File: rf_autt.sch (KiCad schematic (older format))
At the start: 10 parts

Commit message: Fix grounding in rf autt
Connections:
- net labels removed: GNDD
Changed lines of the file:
@@
 $Descr A4 11693 8268
 encoding utf-8
-Sheet 8 9
+Sheet 7 7
 Title "HF-SDR RF-Attenuator"
 Date "2020 december"
@@
 F 3 "" H 5600 4400 50  0001 C CNN
 	1    5600 4400
-	1    0    0    -1
-$EndComp
-$Comp
-L power:GNDD #PWR?
-U 1 1 5FE533AF
-P 5600 2700
-F 0 "#PWR?" H 5600 2450 50  0001 C CNN
-F 1 "GNDD" H 5604 2545 50  0000 C CNN
-F 2 "" H 5600 2700 50  0001 C CNN
-F 3 "" H 5600 2700 50  0001 C CNN
-	1    5600 2700
 	1    0    0    -1
 $EndComp
@@
 Wire Wire Line
 	5150 1400 4400 1400
-$Comp
-L power:GNDD #PWR?
-U 1 1 5FECD05D
-P 6300 1550
-F 0 "#PWR?" H 6300 1300 50  0001 C CNN
-F 1 "GNDD" H 6304 1395 50  0000 C CNN
-F 2 "" H 6300 1550 50  0001 C CNN
-F 3 "" H 6300 1550 50  0001 C CNN
-	1    6300 1550
-	1    0    0    -1
-$EndComp
 Wire Wire Line
 	6300 1550 6300 1400
@@
 Wire Wire Line
 	6050 1550 6300 1550
-Connection ~ 6300 1550
 Text Notes 4350 1150 0    50   ~ 0
 S0    S1    Att\n\n 0     0     0dB\n 0     1    10dB\n 1     0    20dB\n 1     1    30dB
@@
 Wire Bus Line
 	4400 2150 4400 6050
+$Comp
+L power:GNDA #PWR?
+U 1 1 5FF9D7B5
+P 5600 2700
+F 0 "#PWR?" H 5600 2450 50  0001 C CNN
+F 1 "GNDA" H 5605 2527 50  0000 C CNN
+F 2 "" H 5600 2700 50  0001 C CNN
+F 3 "" H 5600 2700 50  0001 C CNN
+	1    5600 2700
+	1    0    0    -1
+$EndComp
+$Comp
+L power:GNDA #PWR?
+U 1 1 5FF9DC72
+P 6300 1550
+F 0 "#PWR?" H 6300 1300 50  0001 C CNN
+F 1 "GNDA" H 6305 1377 50  0000 C CNN
+F 2 "" H 6300 1550 50  0001 C CNN
+F 3 "" H 6300 1550 50  0001 C CNN
+	1    6300 1550
+	1    0    0    -1
+$EndComp
+Connection ~ 6300 1550
 $EndSCHEMATC

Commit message: Initalize receiver test circuit
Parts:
- gave numbers to parts that had none: 10
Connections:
- net labels added: +5VA
- net labels removed: VCC
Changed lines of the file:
@@
 OUT
 $Comp
-L sdr:FST3253 U?
+L sdr:FST3253 U4
 U 1 1 5FE50A6B
 P 5600 1900
-F 0 "U?" H 5350 2550 50  0000 C CNN
+F 0 "U4" H 5350 2550 50  0000 C CNN
 F 1 "FST3253" H 5800 2550 50  0000 C CNN
 F 2 "" H 5600 1900 50  0001 C CNN
@@
 ATT_SEL1
 $Comp
-L power:GNDA #PWR?
+L power:GNDA #PWR0136
 U 1 1 5FE53082
 P 5600 4400
-F 0 "#PWR?" H 5600 4150 50  0001 C CNN
+F 0 "#PWR0136" H 5600 4150 50  0001 C CNN
 F 1 "GNDA" H 5605 4227 50  0000 C CNN
 F 2 "" H 5600 4400 50  0001 C CNN
@@
 $EndComp
 $Comp
-L power:VCC #PWR?
-U 1 1 5FE54C36
-P 5600 1200
-F 0 "#PWR?" H 5600 1050 50  0001 C CNN
-F 1 "VCC" H 5615 1373 50  0000 C CNN
-F 2 "" H 5600 1200 50  0001 C CNN
-F 3 "" H 5600 1200 50  0001 C CNN
-	1    5600 1200
-	1    0    0    -1
-$EndComp
-$Comp
-L Device:R R?
+L Device:R R19
 U 1 1 5FE56E4E
 P 5600 4250
-F 0 "R?" H 5530 4204 50  0000 R CNN
+F 0 "R19" H 5530 4204 50  0000 R CNN
 F 1 "33" H 5530 4295 50  0000 R CNN
 F 2 "" V 5530 4250 50  0001 C CNN
@@
 $EndComp
 $Comp
-L Device:R R?
+L Device:R R16
 U 1 1 5FE5744A
 P 5300 3950
-F 0 "R?" V 5093 3950 50  0000 C CNN
+F 0 "R16" V 5093 3950 50  0000 C CNN
 F 1 "27" V 5184 3950 50  0000 C CNN
 F 2 "" V 5230 3950 50  0001 C CNN
@@
 $EndComp
 $Comp
-L Device:R R?
+L Device:R R22
 U 1 1 5FE57E99
 P 5900 3950
-F 0 "R?" V 5693 3950 50  0000 C CNN
+F 0 "R22" V 5693 3950 50  0000 C CNN
 F 1 "27" V 5784 3950 50  0000 C CNN
 F 2 "" V 5830 3950 50  0001 C CNN
@@
 	5600 3950 5750 3950
 $Comp
-L power:GNDA #PWR?
+L power:GNDA #PWR0137
 U 1 1 5FE5C53B
 P 5600 6600
-F 0 "#PWR?" H 5600 6350 50  0001 C CNN
+F 0 "#PWR0137" H 5600 6350 50  0001 C CNN
 F 1 "GNDA" H 5605 6427 50  0000 C CNN
 F 2 "" H 5600 6600 50  0001 C CNN
@@
 $EndComp
 $Comp
-L Device:R R?
+L Device:R R21
 U 1 1 5FE5C541
 P 5600 6450
-F 0 "R?" H 5530 6404 50  0000 R CNN
+F 0 "R21" H 5530 6404 50  0000 R CNN
 F 1 "3" H 5530 6495 50  0000 R CNN
 F 2 "" V 5530 6450 50  0001 C CNN
@@
 $EndComp
 $Comp
-L Device:R R?
+L Device:R R18
 U 1 1 5FE5C547
 P 5300 6150
-F 0 "R?" V 5093 6150 50  0000 C CNN
+F 0 "R18" V 5093 6150 50  0000 C CNN
 F 1 "47" V 5184 6150 50  0000 C CNN
 F 2 "" V 5230 6150 50  0001 C CNN
@@
 $EndComp
 $Comp
-L Device:R R?
+L Device:R R24
 U 1 1 5FE5C54D
 P 5900 6150
-F 0 "R?" V 5693 6150 50  0000 C CNN
+F 0 "R24" V 5693 6150 50  0000 C CNN
 F 1 "47" V 5784 6150 50  0000 C CNN
 F 2 "" V 5830 6150 50  0001 C CNN
@@
 	5600 6150 5750 6150
 $Comp
-L power:GNDA #PWR?
+L power:GNDA #PWR0138
 U 1 1 5FE5CA2D
 P 5600 5500
-F 0 "#PWR?" H 5600 5250 50  0001 C CNN
+F 0 "#PWR0138" H 5600 5250 50  0001 C CNN
 F 1 "GNDA" H 5605 5327 50  0000 C CNN
 F 2 "" H 5600 5500 50  0001 C CNN
@@
 $EndComp
 $Comp
-L Device:R R?
+L Device:R R20
 U 1 1 5FE5CA33
 P 5600 5350
-F 0 "R?" H 5530 5304 50  0000 R CNN
+F 0 "R20" H 5530 5304 50  0000 R CNN
 F 1 "10" H 5530 5395 50  0000 R CNN
 F 2 "" V 5530 5350 50  0001 C CNN
@@
 $EndComp
 $Comp
-L Device:R R?
+L Device:R R17
 U 1 1 5FE5CA39
 P 5300 5050
-F 0 "R?" V 5093 5050 50  0000 C CNN
+F 0 "R17" V 5093 5050 50  0000 C CNN
 F 1 "39" V 5184 5050 50  0000 C CNN
 F 2 "" V 5230 5050 50  0001 C CNN
@@
 $EndComp
 $Comp
-L Device:R R?
+L Device:R R23
 U 1 1 5FE5CA3F
 P 5900 5050
-F 0 "R?" V 5693 5050 50  0000 C CNN
+F 0 "R23" V 5693 5050 50  0000 C CNN
 F 1 "39" V 5784 5050 50  0000 C CNN
 F 2 "" V 5830 5050 50  0001 C CNN
@@
 Wire Notes Line
 	4300 800  5100 800
+$Comp
+L power:GNDA #PWR0139
+U 1 1 5FF9D7B5
+P 5600 2700
+F 0 "#PWR0139" H 5600 2450 50  0001 C CNN
+F 1 "GNDA" H 5605 2527 50  0000 C CNN
+F 2 "" H 5600 2700 50  0001 C CNN
+F 3 "" H 5600 2700 50  0001 C CNN
+	1    5600 2700
+	1    0    0    -1
+$EndComp
+$Comp
+L power:GNDA #PWR0140
+U 1 1 5FF9DC72
+P 6300 1550
+F 0 "#PWR0140" H 6300 1300 50  0001 C CNN
+F 1 "GNDA" H 6305 1377 50  0000 C CNN
+F 2 "" H 6300 1550 50  0001 C CNN
+F 3 "" H 6300 1550 50  0001 C CNN
+	1    6300 1550
+	1    0    0    -1
+$EndComp
+Connection ~ 6300 1550
+$Comp
+L power:+5VA #PWR0141
+U 1 1 5FF9E701
+P 5600 1200
+F 0 "#PWR0141" H 5600 1050 50  0001 C CNN
+F 1 "+5VA" H 5615 1373 50  0000 C CNN
+F 2 "" H 5600 1200 50  0001 C CNN
+F 3 "" H 5600 1200 50  0001 C CNN
+	1    5600 1200
+	1    0    0    -1
+$EndComp
 Wire Bus Line
 	6850 2150 6850 6050
 Wire Bus Line
 	4400 2150 4400 6050
-$Comp
-L power:GNDA #PWR?
-U 1 1 5FF9D7B5
-P 5600 2700
-F 0 "#PWR?" H 5600 2450 50  0001 C CNN
-F 1 "GNDA" H 5605 2527 50  0000 C CNN
-F 2 "" H 5600 2700 50  0001 C CNN
-F 3 "" H 5600 2700 50  0001 C CNN
-	1    5600 2700
-	1    0    0    -1
-$EndComp
-$Comp
-L power:GNDA #PWR?
-U 1 1 5FF9DC72
-P 6300 1550
-F 0 "#PWR?" H 6300 1300 50  0001 C CNN
-F 1 "GNDA" H 6305 1377 50  0000 C CNN
-F 2 "" H 6300 1550 50  0001 C CNN
-F 3 "" H 6300 1550 50  0001 C CNN
-	1    6300 1550
-	1    0    0    -1
-$EndComp
-Connection ~ 6300 1550
 $EndSCHEMATC

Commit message: Nyáktervezésre majdnem kész
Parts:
- R16, R17, R18, R19, R20, R21, R22, R23, R24: footprint (none) -> Resistor_SMD:R_0805_2012Metric_Pad1.15x1.40mm_HandSolder
- U4: footprint (none) -> Package_SO:TSSOP-16_4.4x5mm_P0.65mm
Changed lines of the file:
@@
 F 0 "U4" H 5350 2550 50  0000 C CNN
 F 1 "FST3253" H 5800 2550 50  0000 C CNN
-F 2 "" H 5600 1900 50  0001 C CNN
+F 2 "Package_SO:TSSOP-16_4.4x5mm_P0.65mm" H 5600 1900 50  0001 C CNN
 F 3 "" H 5600 1900 50  0001 C CNN
 	1    5600 1900
@@
 F 0 "R19" H 5530 4204 50  0000 R CNN
 F 1 "33" H 5530 4295 50  0000 R CNN
-F 2 "" V 5530 4250 50  0001 C CNN
+F 2 "Resistor_SMD:R_0805_2012Metric_Pad1.15x1.40mm_HandSolder" V 5530 4250 50  0001 C CNN
 F 3 "~" H 5600 4250 50  0001 C CNN
 	1    5600 4250
@@
 F 0 "R16" V 5093 3950 50  0000 C CNN
 F 1 "27" V 5184 3950 50  0000 C CNN
-F 2 "" V 5230 3950 50  0001 C CNN
+F 2 "Resistor_SMD:R_0805_2012Metric_Pad1.15x1.40mm_HandSolder" V 5230 3950 50  0001 C CNN
 F 3 "~" H 5300 3950 50  0001 C CNN
 	1    5300 3950
@@
 F 0 "R22" V 5693 3950 50  0000 C CNN
 F 1 "27" V 5784 3950 50  0000 C CNN
-F 2 "" V 5830 3950 50  0001 C CNN
+F 2 "Resistor_SMD:R_0805_2012Metric_Pad1.15x1.40mm_HandSolder" V 5830 3950 50  0001 C CNN
 F 3 "~" H 5900 3950 50  0001 C CNN
 	1    5900 3950
@@
 F 0 "R21" H 5530 6404 50  0000 R CNN
 F 1 "3" H 5530 6495 50  0000 R CNN
-F 2 "" V 5530 6450 50  0001 C CNN
+F 2 "Resistor_SMD:R_0805_2012Metric_Pad1.15x1.40mm_HandSolder" V 5530 6450 50  0001 C CNN
 F 3 "~" H 5600 6450 50  0001 C CNN
 	1    5600 6450
@@
 F 0 "R18" V 5093 6150 50  0000 C CNN
 F 1 "47" V 5184 6150 50  0000 C CNN
-F 2 "" V 5230 6150 50  0001 C CNN
+F 2 "Resistor_SMD:R_0805_2012Metric_Pad1.15x1.40mm_HandSolder" V 5230 6150 50  0001 C CNN
 F 3 "~" H 5300 6150 50  0001 C CNN
 	1    5300 6150
@@
 F 0 "R24" V 5693 6150 50  0000 C CNN
 F 1 "47" V 5784 6150 50  0000 C CNN
-F 2 "" V 5830 6150 50  0001 C CNN
+F 2 "Resistor_SMD:R_0805_2012Metric_Pad1.15x1.40mm_HandSolder" V 5830 6150 50  0001 C CNN
 F 3 "~" H 5900 6150 50  0001 C CNN
 	1    5900 6150
@@
 F 0 "R20" H 5530 5304 50  0000 R CNN
 F 1 "10" H 5530 5395 50  0000 R CNN
-F 2 "" V 5530 5350 50  0001 C CNN
+F 2 "Resistor_SMD:R_0805_2012Metric_Pad1.15x1.40mm_HandSolder" V 5530 5350 50  0001 C CNN
 F 3 "~" H 5600 5350 50  0001 C CNN
 	1    5600 5350
@@
 F 0 "R17" V 5093 5050 50  0000 C CNN
 F 1 "39" V 5184 5050 50  0000 C CNN
-F 2 "" V 5230 5050 50  0001 C CNN
+F 2 "Resistor_SMD:R_0805_2012Metric_Pad1.15x1.40mm_HandSolder" V 5230 5050 50  0001 C CNN
 F 3 "~" H 5300 5050 50  0001 C CNN
 	1    5300 5050
@@
 F 0 "R23" V 5693 5050 50  0000 C CNN
 F 1 "39" V 5784 5050 50  0000 C CNN
-F 2 "" V 5830 5050 50  0001 C CNN
+F 2 "Resistor_SMD:R_0805_2012Metric_Pad1.15x1.40mm_HandSolder" V 5830 5050 50  0001 C CNN
 F 3 "~" H 5900 5050 50  0001 C CNN
 	1    5900 5050

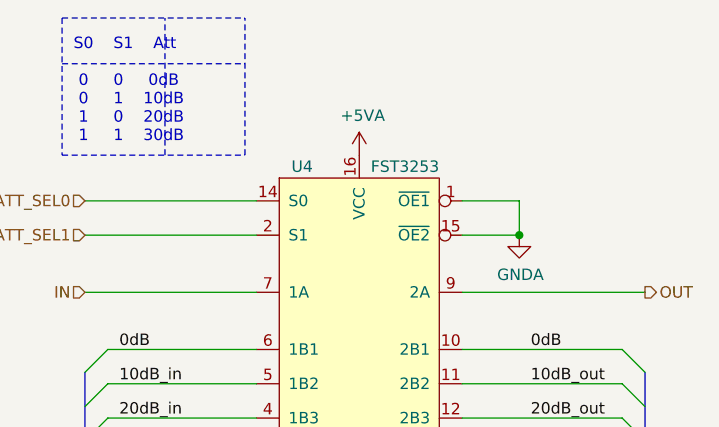
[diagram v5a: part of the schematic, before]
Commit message: Add part number to auttenator
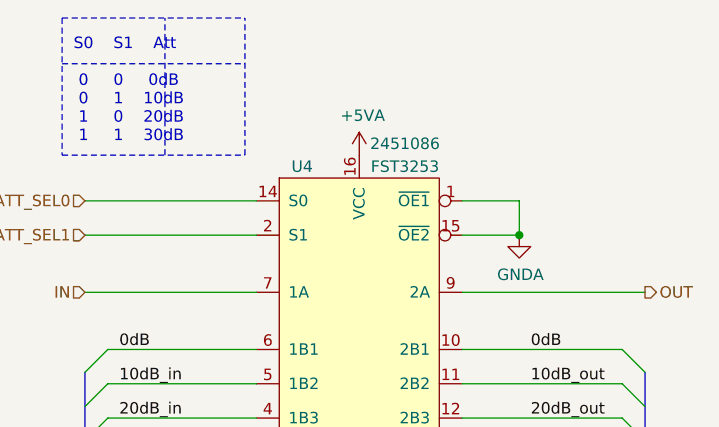
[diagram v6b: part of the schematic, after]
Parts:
- U4: Farnell (none) -> 2451086
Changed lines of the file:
@@
 F 2 "Package_SO:TSSOP-16_4.4x5mm_P0.65mm" H 5600 1900 50  0001 C CNN
 F 3 "" H 5600 1900 50  0001 C CNN
+F 4 " 2451086 " H 5800 2650 50  0000 C CNN "Farnell"
 	1    5600 1900
 	1    0    0    -1

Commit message: Pcb vHA8KDA
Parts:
- R16, R17, R18, R19, R20, R21, R22, R23, R24: footprint Resistor_SMD:R_0805_2012Metric_Pad1.15x1.40mm_HandSolder -> Resistor_SMD:R_0805_2012Metric_Pad1.20x1.40mm_HandSolder
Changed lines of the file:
@@
 F 0 "R19" H 5530 4204 50  0000 R CNN
 F 1 "33" H 5530 4295 50  0000 R CNN
-F 2 "Resistor_SMD:R_0805_2012Metric_Pad1.15x1.40mm_HandSolder" V 5530 4250 50  0001 C CNN
+F 2 "Resistor_SMD:R_0805_2012Metric_Pad1.20x1.40mm_HandSolder" V 5530 4250 50  0001 C CNN
 F 3 "~" H 5600 4250 50  0001 C CNN
 	1    5600 4250
@@
 F 0 "R16" V 5093 3950 50  0000 C CNN
 F 1 "27" V 5184 3950 50  0000 C CNN
-F 2 "Resistor_SMD:R_0805_2012Metric_Pad1.15x1.40mm_HandSolder" V 5230 3950 50  0001 C CNN
+F 2 "Resistor_SMD:R_0805_2012Metric_Pad1.20x1.40mm_HandSolder" V 5230 3950 50  0001 C CNN
 F 3 "~" H 5300 3950 50  0001 C CNN
 	1    5300 3950
@@
 F 0 "R22" V 5693 3950 50  0000 C CNN
 F 1 "27" V 5784 3950 50  0000 C CNN
-F 2 "Resistor_SMD:R_0805_2012Metric_Pad1.15x1.40mm_HandSolder" V 5830 3950 50  0001 C CNN
+F 2 "Resistor_SMD:R_0805_2012Metric_Pad1.20x1.40mm_HandSolder" V 5830 3950 50  0001 C CNN
 F 3 "~" H 5900 3950 50  0001 C CNN
 	1    5900 3950
@@
 F 0 "R21" H 5530 6404 50  0000 R CNN
 F 1 "3" H 5530 6495 50  0000 R CNN
-F 2 "Resistor_SMD:R_0805_2012Metric_Pad1.15x1.40mm_HandSolder" V 5530 6450 50  0001 C CNN
+F 2 "Resistor_SMD:R_0805_2012Metric_Pad1.20x1.40mm_HandSolder" V 5530 6450 50  0001 C CNN
 F 3 "~" H 5600 6450 50  0001 C CNN
 	1    5600 6450
@@
 F 0 "R18" V 5093 6150 50  0000 C CNN
 F 1 "47" V 5184 6150 50  0000 C CNN
-F 2 "Resistor_SMD:R_0805_2012Metric_Pad1.15x1.40mm_HandSolder" V 5230 6150 50  0001 C CNN
+F 2 "Resistor_SMD:R_0805_2012Metric_Pad1.20x1.40mm_HandSolder" V 5230 6150 50  0001 C CNN
 F 3 "~" H 5300 6150 50  0001 C CNN
 	1    5300 6150
@@
 F 0 "R24" V 5693 6150 50  0000 C CNN
 F 1 "47" V 5784 6150 50  0000 C CNN
-F 2 "Resistor_SMD:R_0805_2012Metric_Pad1.15x1.40mm_HandSolder" V 5830 6150 50  0001 C CNN
+F 2 "Resistor_SMD:R_0805_2012Metric_Pad1.20x1.40mm_HandSolder" V 5830 6150 50  0001 C CNN
 F 3 "~" H 5900 6150 50  0001 C CNN
 	1    5900 6150
@@
 F 0 "R20" H 5530 5304 50  0000 R CNN
 F 1 "10" H 5530 5395 50  0000 R CNN
-F 2 "Resistor_SMD:R_0805_2012Metric_Pad1.15x1.40mm_HandSolder" V 5530 5350 50  0001 C CNN
+F 2 "Resistor_SMD:R_0805_2012Metric_Pad1.20x1.40mm_HandSolder" V 5530 5350 50  0001 C CNN
 F 3 "~" H 5600 5350 50  0001 C CNN
 	1    5600 5350
@@
 F 0 "R17" V 5093 5050 50  0000 C CNN
 F 1 "39" V 5184 5050 50  0000 C CNN
-F 2 "Resistor_SMD:R_0805_2012Metric_Pad1.15x1.40mm_HandSolder" V 5230 5050 50  0001 C CNN
+F 2 "Resistor_SMD:R_0805_2012Metric_Pad1.20x1.40mm_HandSolder" V 5230 5050 50  0001 C CNN
 F 3 "~" H 5300 5050 50  0001 C CNN
 	1    5300 5050
@@
 F 0 "R23" V 5693 5050 50  0000 C CNN
 F 1 "39" V 5784 5050 50  0000 C CNN
-F 2 "Resistor_SMD:R_0805_2012Metric_Pad1.15x1.40mm_HandSolder" V 5830 5050 50  0001 C CNN
+F 2 "Resistor_SMD:R_0805_2012Metric_Pad1.20x1.40mm_HandSolder" V 5830 5050 50  0001 C CNN
 F 3 "~" H 5900 5050 50  0001 C CNN
 	1    5900 5050
